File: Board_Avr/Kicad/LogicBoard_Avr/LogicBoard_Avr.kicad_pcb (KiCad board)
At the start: 4 copper layers, 89.2 x 87.8 mm, 56 parts, among them J1 I2C_Interface, J10 PSU Connector, J11 TriggeredStatusLedConnector, J12 PowerStatusLedConnector, J2 UART_Interface, J3 Mechanical user interface mai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, J4 Power board connector, J5 SPI Connector, J6 ICSP Header, J9 GPIO Connector, SW1 Reset switch, U1 ATmega328PB-A, U2 TLP291, U3 TLV1117-33IDCYRG3, U4 LM1117-5.0, X1 ASV-12.000MHZ-EJ-T, Y1 ABLS-20.000MHz-16-A-4-H-T

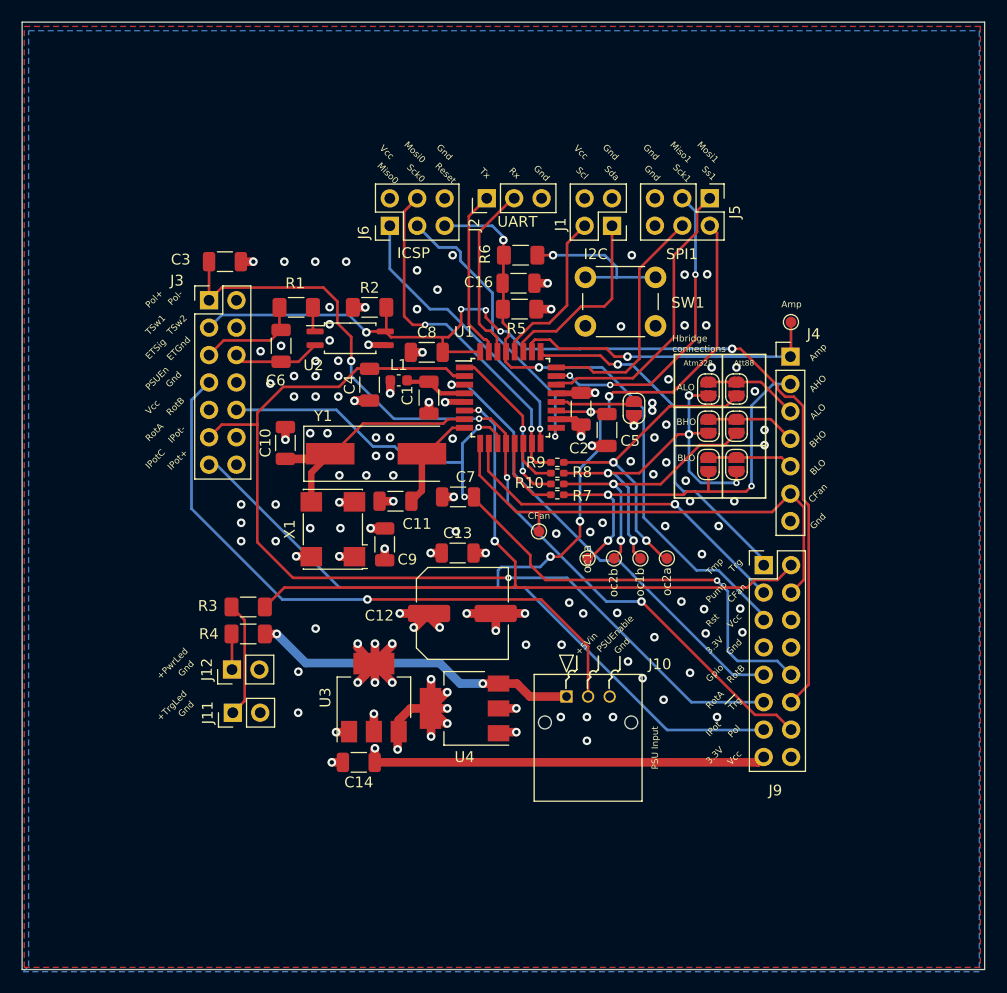
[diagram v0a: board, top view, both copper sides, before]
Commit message: Finalised routing and finalised silkscreen
Signed-off-by: bebenlebricolo <benoittarrade@hotmail.fr>
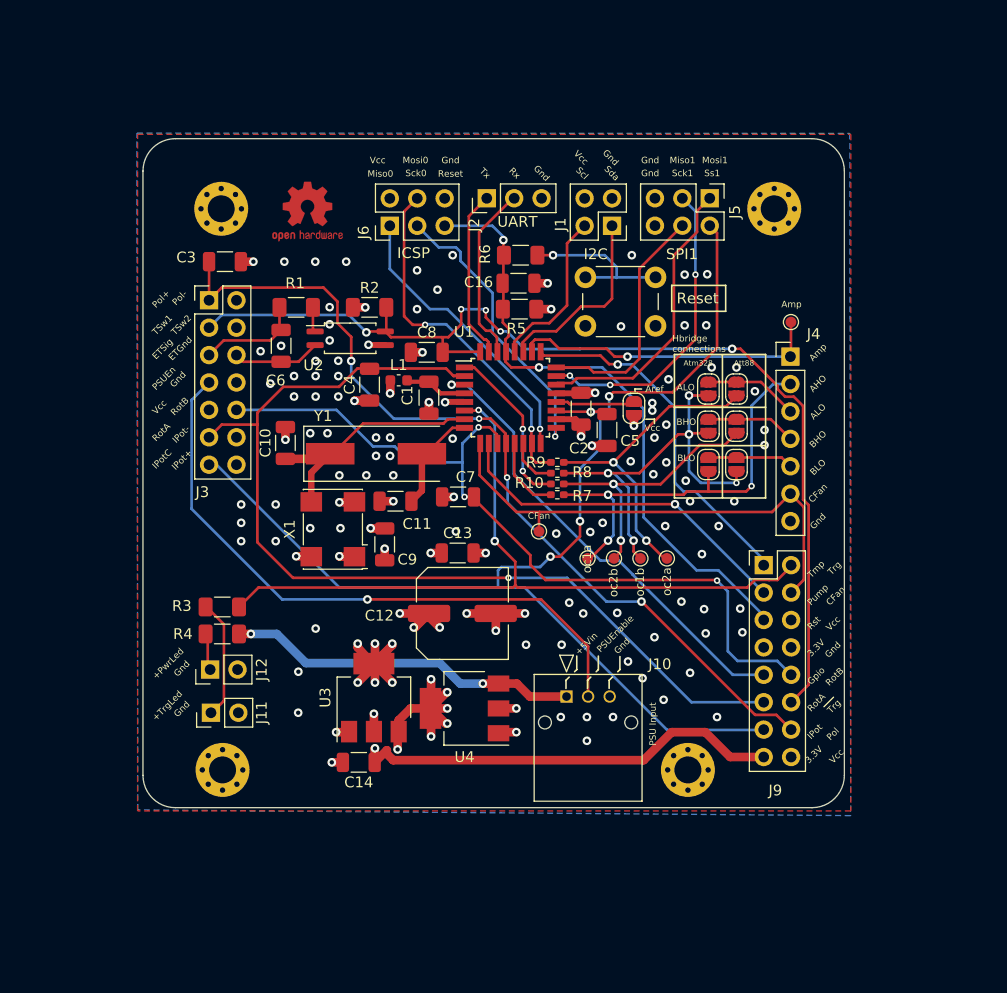
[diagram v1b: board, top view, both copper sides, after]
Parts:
- added H1: MountingHole_Pad, MountingHole:MountingHole_2.5mm_Pad_Via, F.Cu at (123.2, 72.5)
- added H2: MountingHole_Pad, MountingHole:MountingHole_2.5mm_Pad_Via, F.Cu at (174.5, 72.5)
- added H3: MountingHole_Pad, MountingHole:MountingHole_2.5mm_Pad_Via, F.Cu at (166.5, 124.5)
- added H4: MountingHole_Pad, MountingHole:MountingHole_2.5mm_Pad_Via, F.Cu at (123.4, 124.5)
- added REF**: OSHW-Logo2_7.3x6mm_Copper, Symbol:OSHW-Logo2_7.3x6mm_Copper, F.Cu at (131.2, 72.8)
- added REF**: OSHW-Logo2_14.6x12mm_SilkScreen, Symbol:OSHW-Logo2_14.6x12mm_SilkScreen, B.Cu at (149.2, 80.5)
- moved R3 2.40 mm to (123.3, 109.4)
- moved R4 2.40 mm to (123.3, 111.9)
- moved J11 2.03 mm to (122.3, 119.2)
- moved J12 2.03 mm to (122.2, 115.2)
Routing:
- net /3.3V: track 56.5 -> 59.4 mm
- net /Triggered(Out): track 69.7 -> 72.1 mm
- net /5V_PSU: track 30.4 -> 32.8 mm
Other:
- board size 89.2 x 87.8 mm -> 65 x 62 mm
- board text added: "Aref"
- board text added: "Beer Thermoregulation System Logic board based on Avr MCU (Version 0.3.0)"
- board text added: "Designed by Benoit Tarrade (alias bebenlebricolo) 7th jan 2022"
- board text added: "Main repository link : https://github.com/bebenlebricolo/BeerThermoregulationSystem BTS-LogicBoard repository link : https://github.com/bebenlebricolo/BTS-LogicBoard"
- board text added: "My Github link : https://github.com/bebenlebricolo"
- board text added: "This board is the brain of the beer thermoregulation system and allows to control the power board via the power board link connector. It supports both the Attiny88 and Atmega328pb (flexibility due to actual chip's global shortage) and allows 2 different system to be implemented on the same board. It might be extended through the use of the SPI, I2C and UART ports and it features an external therm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"

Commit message: Replaced TLV1117-3.3 by NCP630SN330 and polished a bit zoning
Signed-off-by: bebenlebricolo <benoittarrade@hotmail.fr>
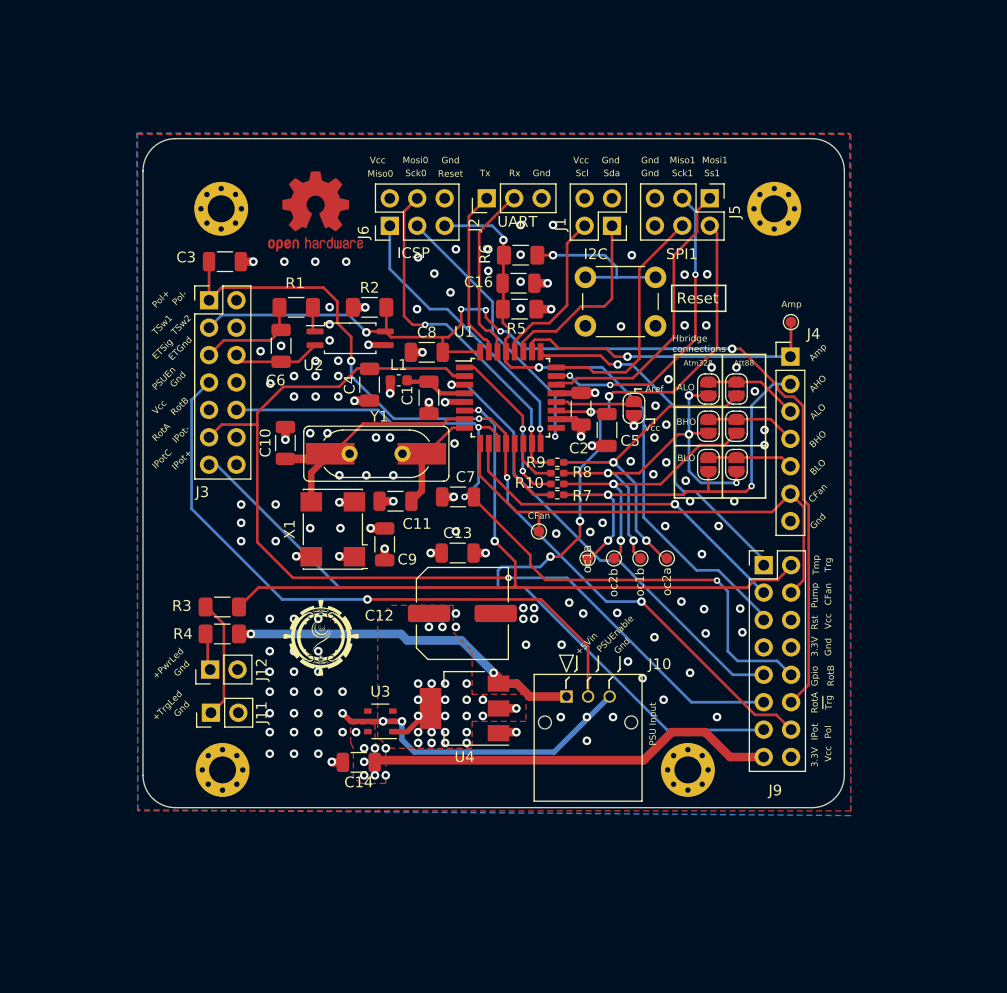
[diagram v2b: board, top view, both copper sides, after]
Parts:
- removed the REF** at (131.2, 72.8)
- removed the REF** at (149.2, 80.5)
- added G***: LOGO, BTS-LogicBoard:Logo, F.Cu at (132.5, 112.2)
- added G***: LOGO, BTS-LogicBoard:Logo_7x7_inv, B.Cu at (130.2, 118.0)
- added REF**: OSHW-Logo2_9.8x8mm_Copper, Symbol:OSHW-Logo2_9.8x8mm_Copper, F.Cu at (132.0, 72.8)
- U3: value TLV1117-33IDCYRG3 -> NCP603SN330T1G; footprint Package_TO_SOT_SMD:SOT-223-3_TabPin2 -> Package_SO:TSOP-5_1.65x3.05mm_P0.95mm
- Y1: footprint Crystal:Crystal_SMD_HC49-SD -> BTS-LogicBoard:Crystal_SMD_TH_Combo_HC49-SD
- moved U3 2.28 mm to (138.0, 120.0), turned to 180 degrees
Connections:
- U3 pad 1: GND -> /VCC
- U3 pad 2: /3.3V -> GND
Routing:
- net GND: track 32.7 -> 53.9 mm, vias 111 -> 139
- net /VCC: track 34.8 -> 15.9 mm, vias 16 -> 31
- net /3.3V: track 59.4 -> 42.1 mm
- net /SCK0(Prog): track 26.6 -> 25.6 mm
- added copper zone on F.Cu, net /3.3V
- added copper zone on F.Cu, net /VCC

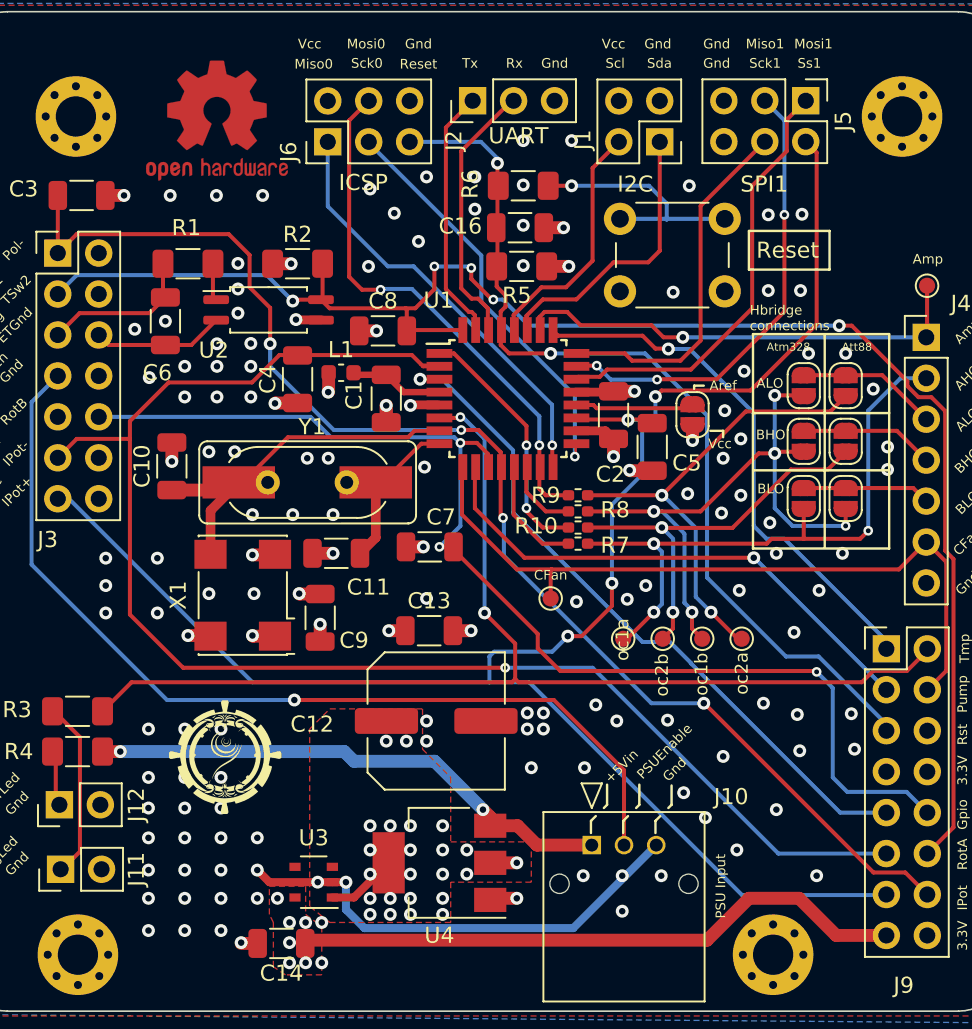
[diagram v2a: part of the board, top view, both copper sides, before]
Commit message: Removed unused pads from vias in order to improve polygons
Signed-off-by: bebenlebricolo <benoittarrade@hotmail.fr>
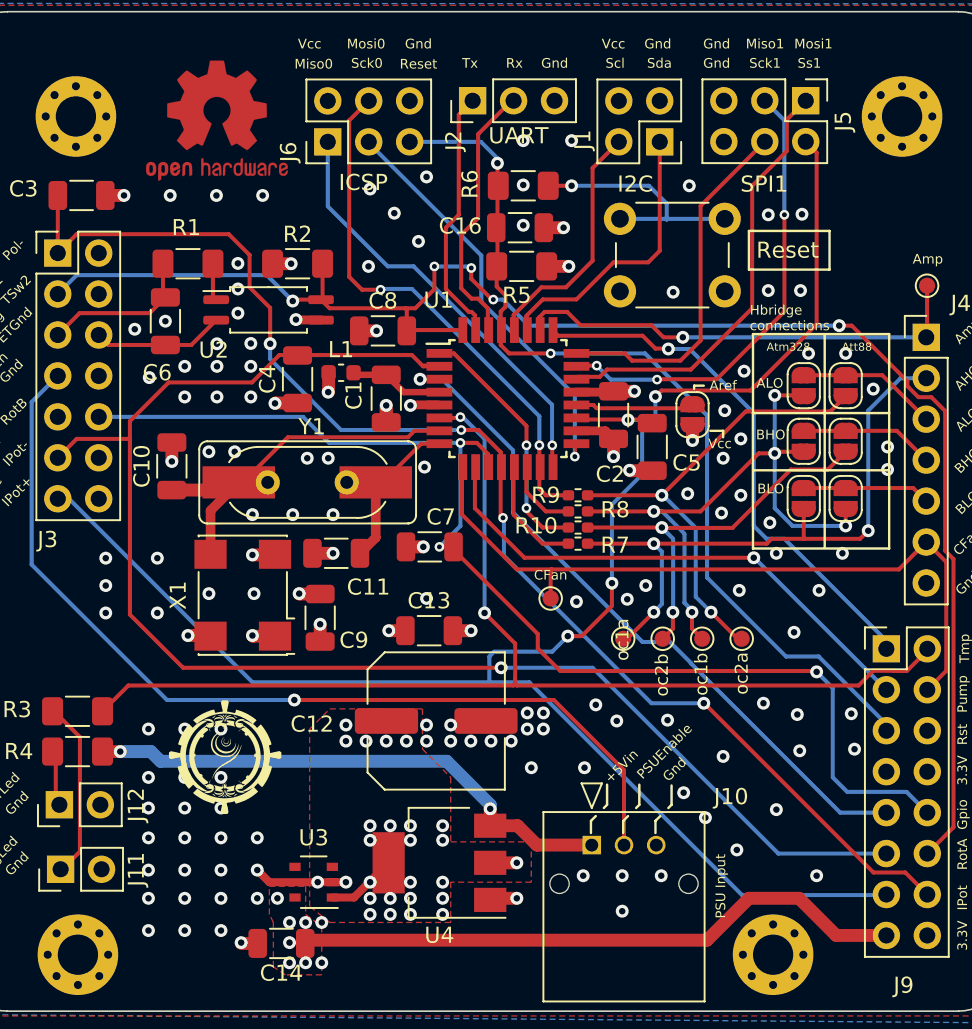
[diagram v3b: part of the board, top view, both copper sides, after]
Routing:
- net GND: track 53.9 -> 30.3 mm, vias 139 -> 141
- net /VCC: vias 31 -> 32

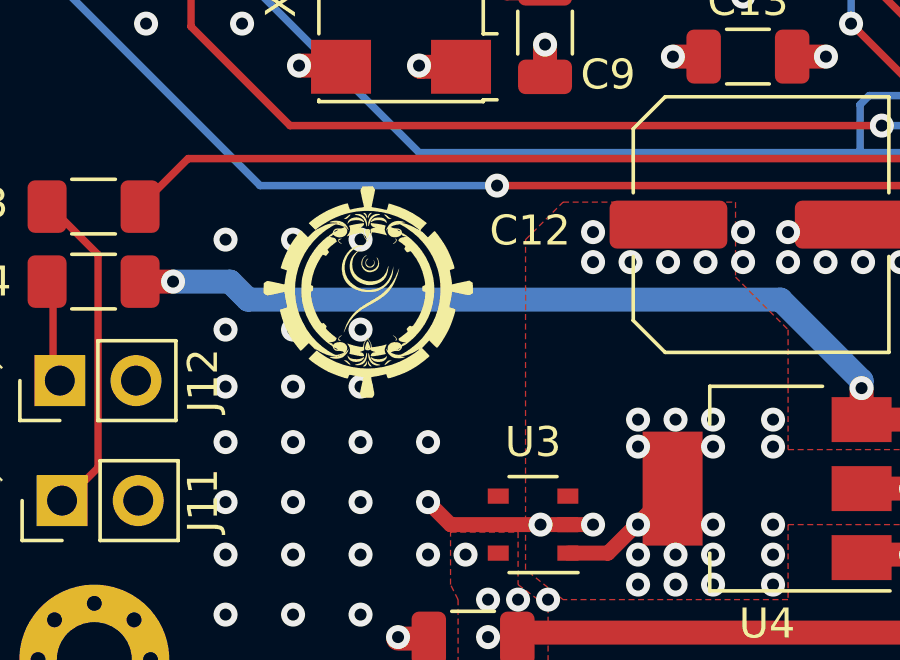
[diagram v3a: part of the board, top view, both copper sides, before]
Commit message: Added BTS logos and updated silkscreen
Signed-off-by: bebenlebricolo <benoittarrade@hotmail.fr>
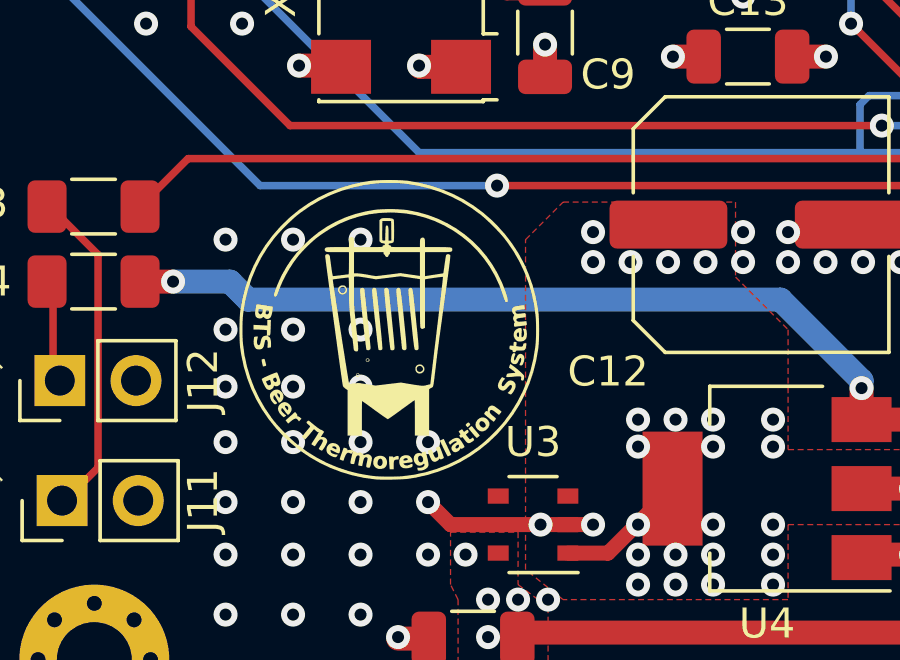
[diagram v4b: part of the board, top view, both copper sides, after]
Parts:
- removed the G*** at (132.5, 112.2)
- removed the G*** at (130.2, 118.0)
- added G***: LOGO, BTS-LogicBoard:BTS-LogoBW-WrappedCircle_10x10mm_silk, F.Cu at (133.2, 113.5)
- added G***: LOGO, BTS-LogicBoard:BTS-LogoBW-WrappedCircle_15x15mm_silk, B.Cu at (148.0, 82.1)
- added REF**: OSHW-Logo2_14.6x12mm_SilkScreen, Symbol:OSHW-Logo2_14.6x12mm_SilkScreen, B.Cu at (131.9, 77.7)
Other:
- board text added: "Beer Thermoregulation System - Logic board (Rev 0.3.0) -"
- board text removed: "Beer Thermoregulation System Logic board based on Avr MCU (Version 0.3.0)"
